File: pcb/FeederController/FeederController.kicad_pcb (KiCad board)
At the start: 4 copper layers, 100 x 100 mm, 92 parts, among them J1 Feeder 1, J10 Feeder 10, J11 Feeder 11, J12 Feeder 12, J13 Feeder 13, J14 Feeder 14, J15 Feeder 15, J16 Feeder 16, J17 12-24v DC, J18 5V Supply, J19 Feeder 17, J2 Feeder 2, J20 Feeder 18, J21 Feeder 19, J22 Feeder 20, J23 Feeder 21, J24 Feeder 22, J25 Feeder 23, J26 Feeder 24, J27 Feeder 25, J28 Feeder 26, J29 Feeder 27, J3 Feeder 3, J30 Feeder 28, J31 Feeder 29, J32 Feeder 30, J33 Feeder 31, J34 Feeder 32, J4 Feeder 4, J5 Feeder 5, J6 Feeder 6, J7 Feeder 7, J8 Feeder 8, J9 Feeder 9, Q1 DMP3028LK3-13, U1 ESP32-Module, U2 PCA9685PW, U3 MCP23017, U4 AP2114-3.3, U5 AP63205WU, U6 PCA9685PW, U7 MCP23017_ML

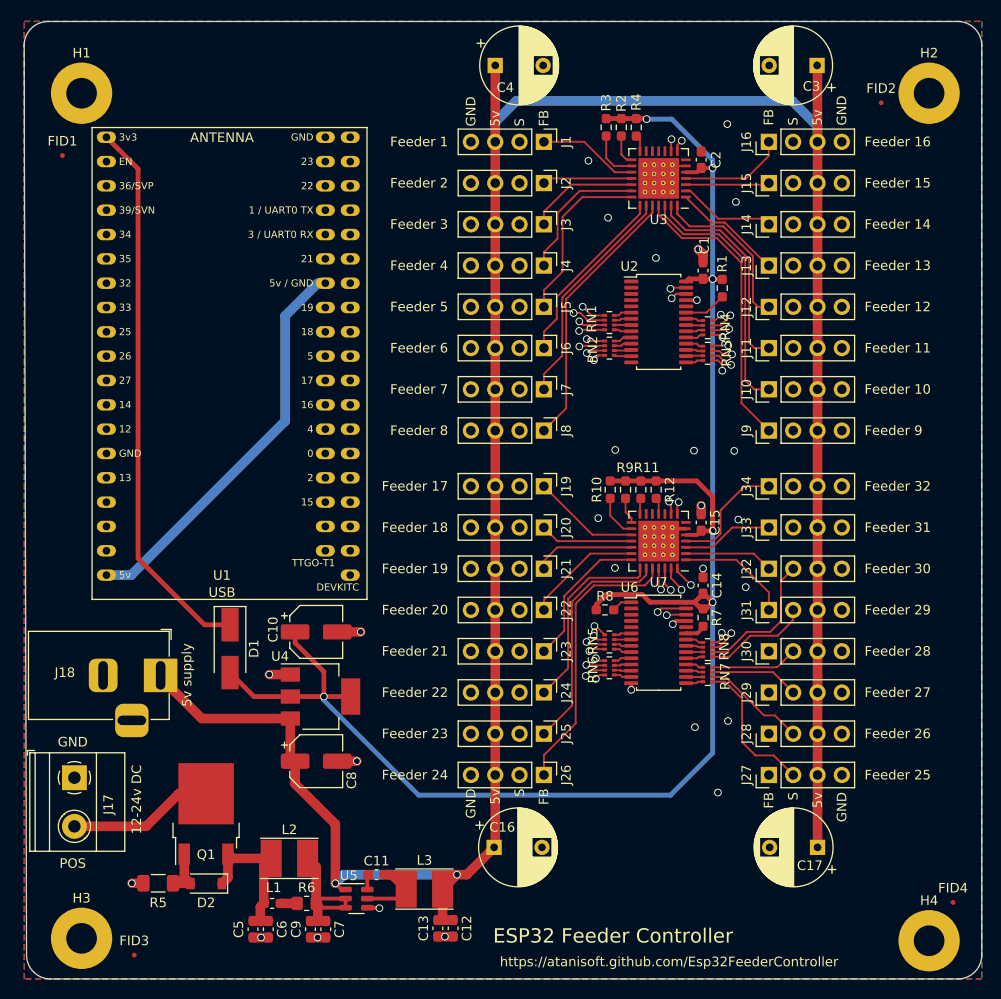
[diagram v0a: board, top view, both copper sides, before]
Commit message: Update PCB as below
* Adjusted placement of mounting holes to line up with LumenPnP staging plate.
* Added 2k4 P/U for SDA/SCL.
* GND plane stitching
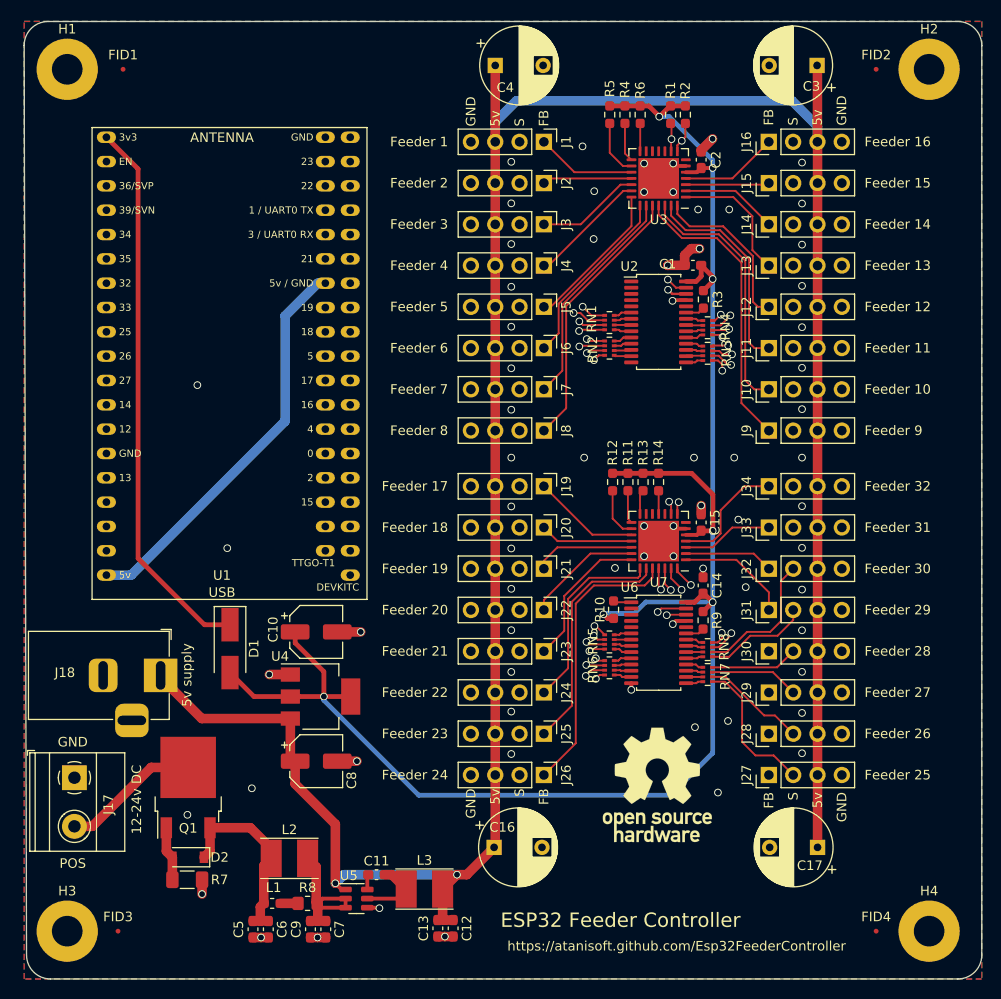
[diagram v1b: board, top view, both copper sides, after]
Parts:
- added R13: 10K, Resistor_SMD:R_0603_1608Metric_Pad0.98x0.95mm_HandSolder, F.Cu at (170.1, 91.1)
- added R14: 10K, Resistor_SMD:R_0603_1608Metric_Pad0.98x0.95mm_HandSolder, F.Cu at (171.8, 91.1)
- added REF**: OSHW-Logo_11.4x12mm_SilkScreen, Symbol:OSHW-Logo_11.4x12mm_SilkScreen, F.Cu at (171.6, 122.7)
- R1, R2: value 10K -> 2k4
- R5: value 100k -> 10K; footprint Resistor_SMD:R_1206_3216Metric_Pad1.30x1.75mm_HandSolder -> Resistor_SMD:R_0603_1608Metric_Pad0.98x0.95mm_HandSolder
- R6: value 0R5 -> 10K; footprint Resistor_SMD:R_0805_2012Metric_Pad1.20x1.40mm_HandSolder -> Resistor_SMD:R_0603_1608Metric_Pad0.98x0.95mm_HandSolder
- R7: value 10K -> 100k; footprint Resistor_SMD:R_0603_1608Metric_Pad0.98x0.95mm_HandSolder -> Resistor_SMD:R_1206_3216Metric_Pad1.30x1.75mm_HandSolder
- R8: value 10K -> 0R5; footprint Resistor_SMD:R_0603_1608Metric_Pad0.98x0.95mm_HandSolder -> Resistor_SMD:R_0805_2012Metric_Pad1.20x1.40mm_HandSolder
- U3, U7: footprint Package_DFN_QFN:QFN-28-1EP_6x6mm_P0.65mm_EP4.25x4.25mm_ThermalVias -> Package_DFN_QFN:QFN-28-1EP_6x6mm_P0.65mm_EP4.25x4.25mm
- moved R5 93.1 mm to (166.7, 52.7), turned to -90 degrees
- moved R6 89.4 mm to (169.8, 52.7), turned to -90 degrees
- moved R7 60.4 mm to (122.5, 132.6), turned to 180 degrees
- moved R8 43.6 mm to (135.1, 135.1)
- moved R3 20.6 mm to (176.4, 72.0)
- moved R1 18.9 mm to (173.0, 52.7)
- moved R9 15.9 mm to (176.4, 105.5)
- moved R10 12.5 mm to (167.1, 104.4), turned to 90 degrees
- moved FID1 11.0 mm to (115.8, 48.0)
- moved FID4 8.57 mm to (194.5, 138.0)
- moved R2 6.82 mm to (174.6, 52.7)
- moved R12 4.62 mm to (166.9, 91.1)
- moved FID2 3.54 mm to (194.5, 48.0)
- moved D2 3.33 mm to (122.6, 130.3)
- moved Q1 3.33 mm to (122.6, 123.0)
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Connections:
- R1 pad 2: Net-(R1-Pad2) -> /SDA
- R2 pad 2: Net-(R2-Pad2) -> /SCL
- R5 pad 1: GND -> +3V3
- R5 pad 2: Net-(D2-Pad2) -> Net-(R5-Pad2)
- R6 pad 1: Net-(L1-Pad2) -> +3V3
- R6 pad 2: Net-(C7-Pad1) -> Net-(R6-Pad2)
- R7 pad 1: +3V3 -> GND
- R7 pad 2: Net-(R7-Pad2) -> Net-(D2-Pad2)
- R8 pad 1: +3V3 -> Net-(L1-Pad2)
- R8 pad 2: Net-(R8-Pad2) -> Net-(C7-Pad1)
- U2 pad 23: Net-(R1-Pad2) -> Net-(R3-Pad2)
- U3 pad 14: Net-(R4-Pad2) -> Net-(R6-Pad2)
- U3 pad 15: Net-(R2-Pad2) -> Net-(R4-Pad2)
- U3 pad 16: Net-(R3-Pad2) -> Net-(R5-Pad2)
- U6 pad 1: Net-(R8-Pad2) -> Net-(R10-Pad2)
- U6 pad 23: Net-(R7-Pad2) -> Net-(R9-Pad2)
- U7 pad 11: Net-(R12-Pad2) -> Net-(R14-Pad2)
- U7 pad 14: Net-(R11-Pad2) -> Net-(R13-Pad2)
- U7 pad 15: Net-(R9-Pad2) -> Net-(R11-Pad2)
- U7 pad 16: Net-(R10-Pad2) -> Net-(R12-Pad2)
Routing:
- net +3V3: track 184.9 -> 192.5 mm, vias 6 -> 7
- net Net-(R5-Pad2): track 0.00 -> 5.91 mm
- net Net-(R1-Pad2): track 4.46 -> 0.00 mm
- net VDD: track 16.7 -> 20.3 mm
- net Net-(R12-Pad2): track 1.73 -> 5.31 mm
- net GND: track 28.2 -> 31.7 mm, vias 29 -> 72
- net Net-(R3-Pad2): track 5.29 -> 2.00 mm
- net Net-(R2-Pad2): track 3.22 -> 0.00 mm
- net Net-(R6-Pad2): track 0.00 -> 2.92 mm
- net Net-(R10-Pad2): track 4.58 -> 1.90 mm
- net /ServoControl (1-16)/feeder-5-feedback: track 18.2 -> 15.7 mm
- net Net-(R13-Pad2): track 0.00 -> 2.55 mm
- net Net-(R14-Pad2): track 0.00 -> 2.42 mm
- net /ServoControl (1-16)/feeder-4-feedback: track 14.7 -> 12.4 mm
- net Net-(R4-Pad2): track 1.75 -> 4.09 mm
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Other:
- board text added: "Mounting holes are centered at 90mm apart in all directions. This allows easy mounting to the LumenPnP staging plate."

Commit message: Added a few DNP footprints for connecting two PCBs together using a single ESP32
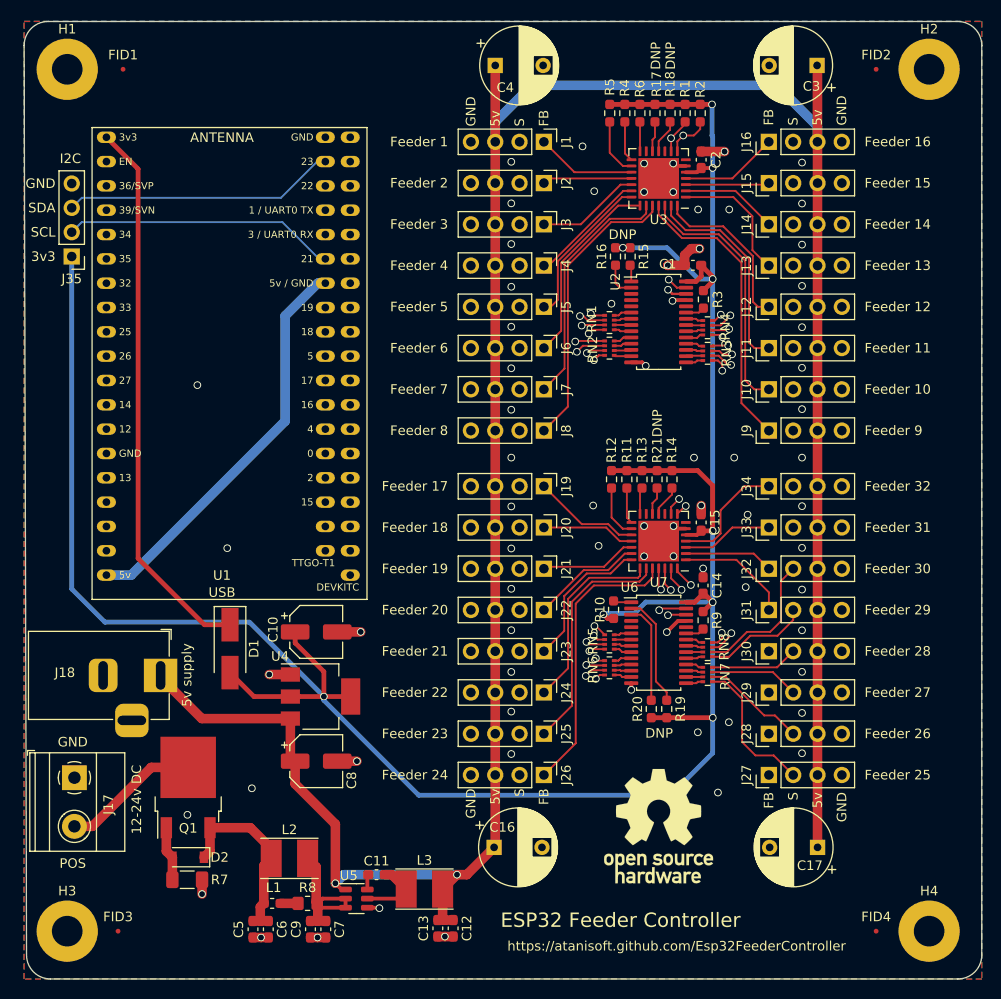
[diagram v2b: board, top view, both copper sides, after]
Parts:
- added J35: EXT-I2C, Connector_PinHeader_2.54mm:PinHeader_1x04_P2.54mm_Vertical, F.Cu at (110.5, 67.5)
- added R15: 10K, Resistor_SMD:R_0603_1608Metric_Pad0.98x0.95mm_HandSolder, F.Cu at (168.8, 67.5)
- added R16: 10K, Resistor_SMD:R_0603_1608Metric_Pad0.98x0.95mm_HandSolder, F.Cu at (167.2, 67.5)
- added R17: 10K, Resistor_SMD:R_0603_1608Metric_Pad0.98x0.95mm_HandSolder, F.Cu at (171.4, 52.6)
- added R18: 10K, Resistor_SMD:R_0603_1608Metric_Pad0.98x0.95mm_HandSolder, F.Cu at (172.9, 52.6)
- added R19: 10K, Resistor_SMD:R_0603_1608Metric_Pad0.98x0.95mm_HandSolder, F.Cu at (172.6, 114.8)
- added R20: 10K, Resistor_SMD:R_0603_1608Metric_Pad0.98x0.95mm_HandSolder, F.Cu at (171.0, 114.8)
- added R21: 10K, Resistor_SMD:R_0603_1608Metric_Pad0.98x0.95mm_HandSolder, F.Cu at (171.6, 90.8)
- moved REF** 4.31 mm to (171.7, 127.0)
- moved R2 1.56 mm to (176.1, 52.6)
- moved R1 1.52 mm to (174.5, 52.6)
- moved R14 1.43 mm to (173.2, 90.8)
- moved R11 0.30 mm to (168.4, 90.8)
- moved R12 0.30 mm to (166.8, 90.8)
- moved R13 0.30 mm to (170.0, 90.8)
- moved R6 0.16 mm to (169.8, 52.6)
- moved R4 0.16 mm to (168.2, 52.6)
- moved R5 0.16 mm to (166.7, 52.6)
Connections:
- U2 pad 1: unconnected-(U2-Pad1) -> Net-(U2-Pad1)
- U2 pad 2: unconnected-(U2-Pad2) -> Net-(U2-Pad2)
- U3 pad 11: unconnected-(U3-Pad11) -> Net-(U3-Pad11)
- U3 pad 12: unconnected-(U3-Pad12) -> Net-(U3-Pad12)
- U6 pad 2: unconnected-(U6-Pad2) -> Net-(U6-Pad2)
- U6 pad 3: unconnected-(U6-Pad3) -> Net-(U6-Pad3)
- U7 pad 12: unconnected-(U7-Pad12) -> Net-(U7-Pad12)
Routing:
- net +3V3: track 192.5 -> 277.9 mm, vias 7 -> 9
- net /SCL: track 118.4 -> 149.9 mm
- net /SDA: track 100.8 -> 131.2 mm
- net Net-(U6-Pad2): track 0.00 -> 11.7 mm
- net Net-(U6-Pad3): track 0.00 -> 10.4 mm
- net Net-(U2-Pad2): track 0.00 -> 3.72 mm
- net Net-(U3-Pad11): track 0.00 -> 3.56 mm
- net GND: track 31.7 -> 34.9 mm, vias 72 -> 73
- net Net-(U3-Pad12): track 0.00 -> 3.18 mm
- net Net-(U7-Pad12): track 0.00 -> 2.90 mm
- net /ServoControl (1-16)/feeder-7-feedback: track 23.6 -> 25.5 mm
- net /ServoControl (1-16)/feeder-8-feedback: track 28.2 -> 30.1 mm
- net Net-(U2-Pad1): track 0.00 -> 1.74 mm
- net +5V: track 264.0 -> 265.4 mm
- net /ServoControl (1-16)/feeder-6-feedback: track 19.0 -> 20.4 mm
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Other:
- board text added: "3v3"
- board text added: "DNP"
- board text added: "I2C"
- board text added: "SCL"
- board text added: "SDA"
